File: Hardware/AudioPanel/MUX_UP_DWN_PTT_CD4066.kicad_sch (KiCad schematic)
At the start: 26 parts, among them SW8 ~{RESET}, U30 MCP23017_ML, U40 4066, U41 4066, U42 4066, U43 4066, U44 4066, U45 4066, U59 4066, U60 MCP23017_ML

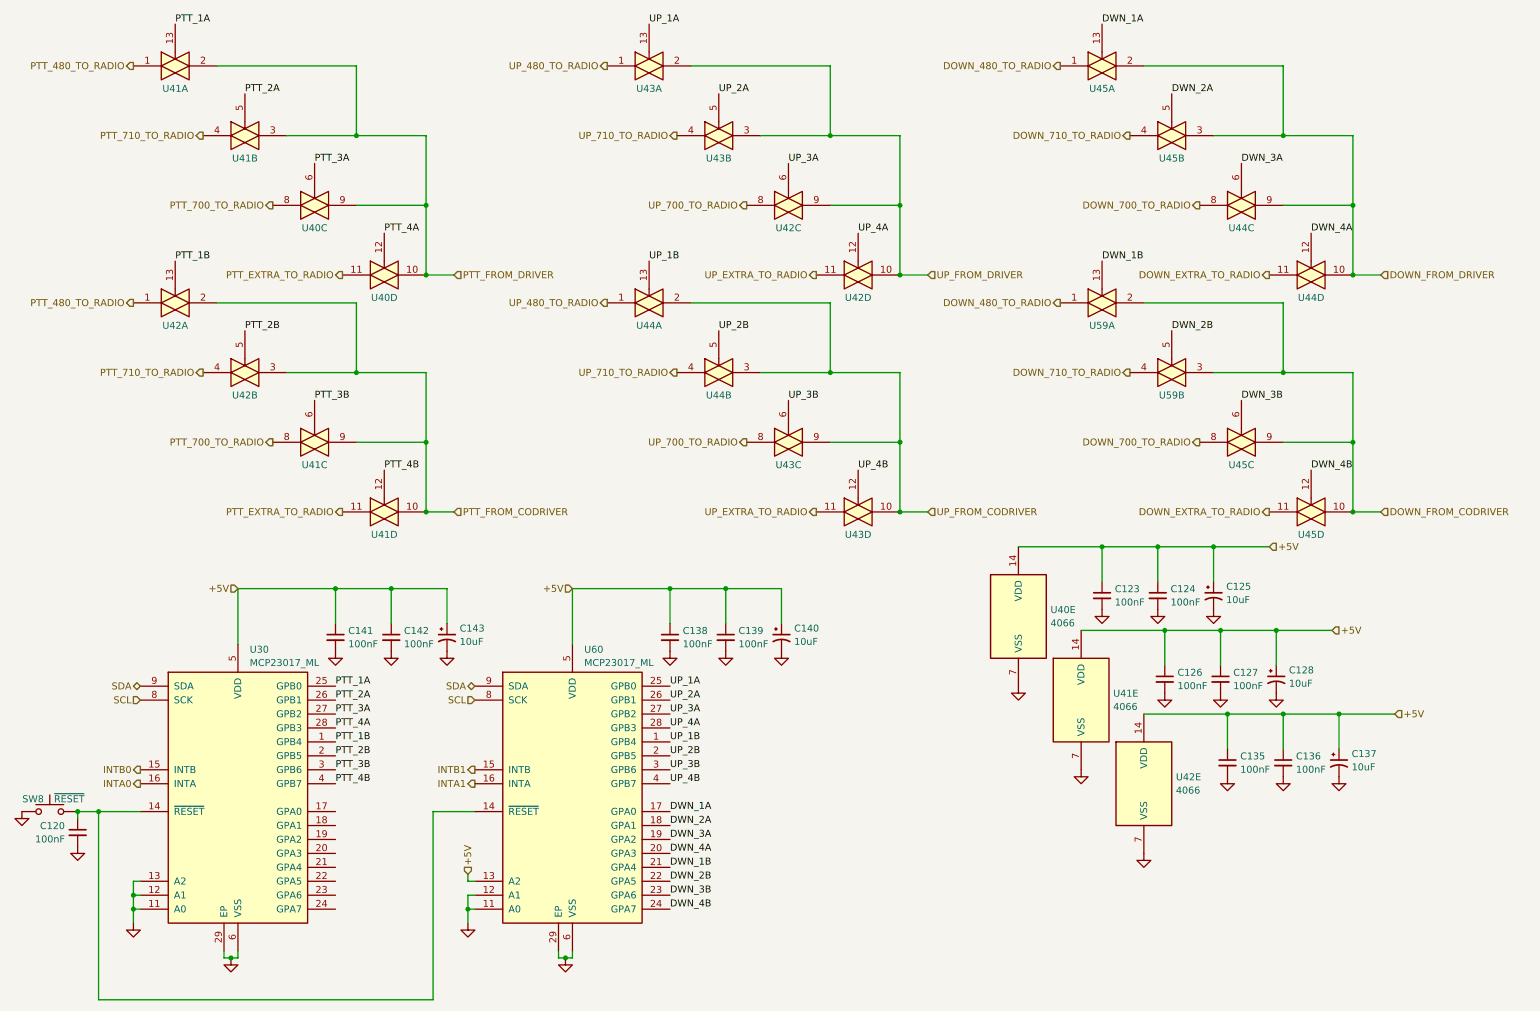
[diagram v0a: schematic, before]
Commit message: Added MIC port protection
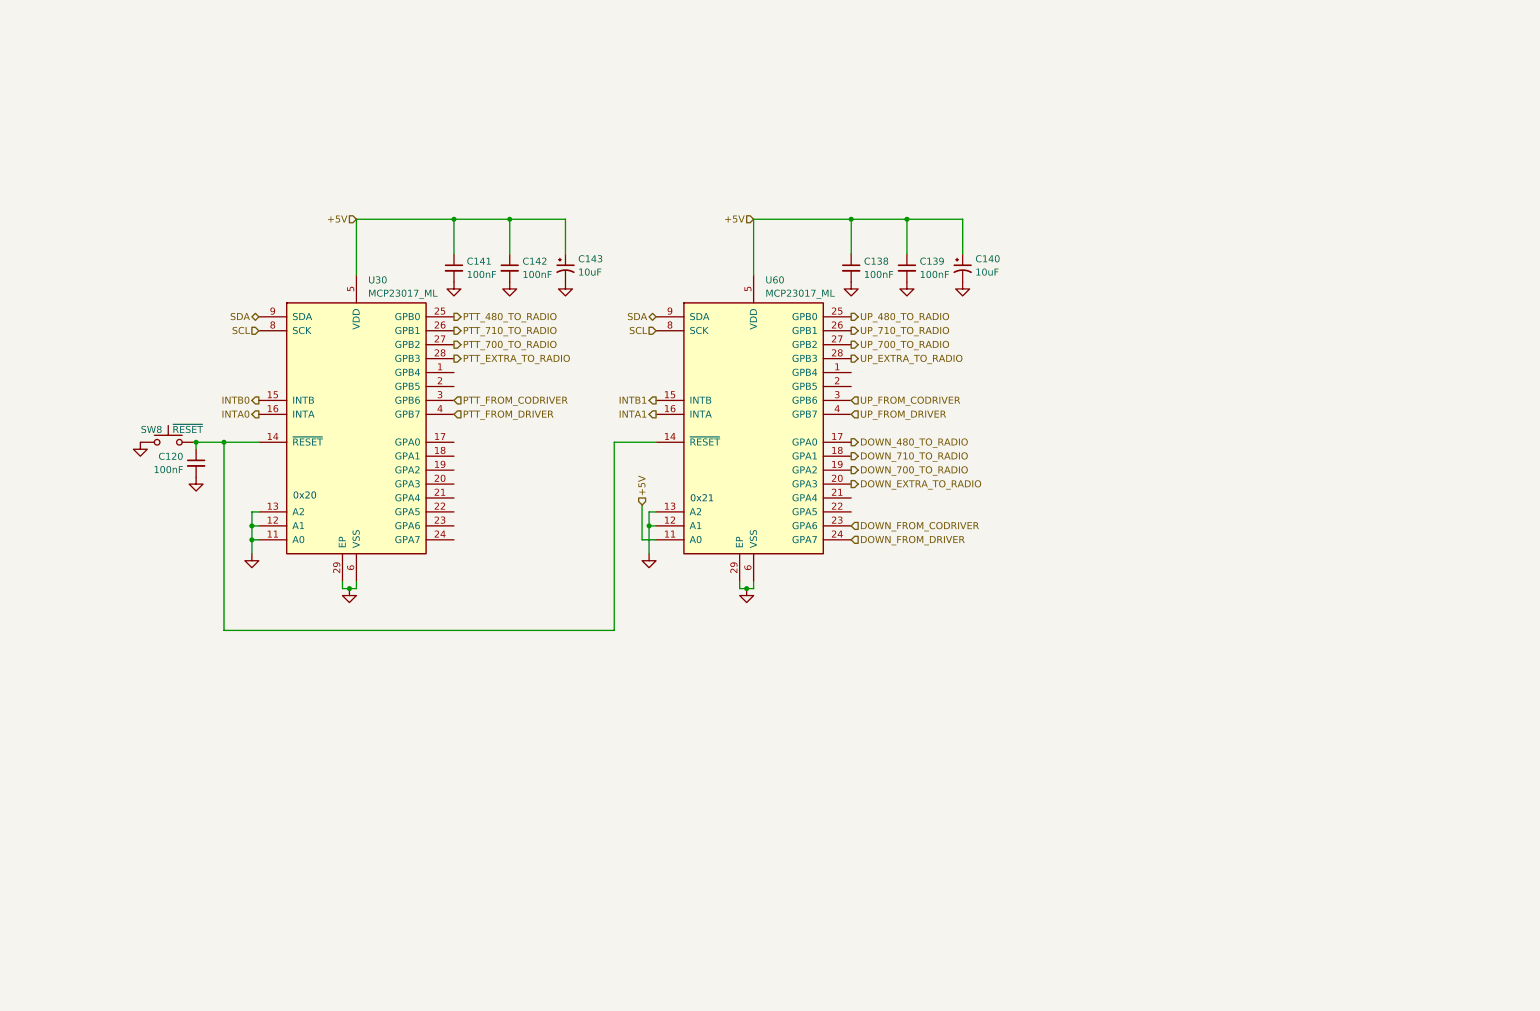
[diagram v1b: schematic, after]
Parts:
- removed C123, C124, C126, C127, C135, C136: 100nF, symbol Device:C_Small
- removed C125, C128, C137: 10uF, symbol Device:C_Polarized_Small_US
- removed U40, U41, U42, U43, U44, U45, U59: 4066, symbol 4xxx:4066
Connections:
- net DWN_1A is gone; now on net DOWN_480_TO_RADIO: U60.17 (GPA0)
- net DWN_2A is gone; now on net DOWN_710_TO_RADIO: U60.18 (GPA1)
- net DWN_3A is gone; now on net DOWN_700_TO_RADIO: U60.19 (GPA2)
- net DWN_3B is gone; now on net DOWN_FROM_CODRIVER: U60.23 (GPA6)
- net DWN_4A is gone; now on net DOWN_EXTRA_TO_RADIO: U60.20 (GPA3)
- net DWN_4B is gone; now on net DOWN_FROM_DRIVER: U60.24 (GPA7)
- net PTT_1A is gone; now on net PTT_480_TO_RADIO: U30.25 (GPB0)
- net PTT_2A is gone; now on net PTT_710_TO_RADIO: U30.26 (GPB1)
- net PTT_3A is gone; now on net PTT_700_TO_RADIO: U30.27 (GPB2)
- net PTT_3B is gone; now on net PTT_FROM_CODRIVER: U30.3 (GPB6)
- net PTT_4A is gone; now on net PTT_EXTRA_TO_RADIO: U30.28 (GPB3)
- net PTT_4B is gone; now on net PTT_FROM_DRIVER: U30.4 (GPB7)
- net UP_1A is gone; now on net UP_480_TO_RADIO: U60.25 (GPB0)
- net UP_2A is gone; now on net UP_710_TO_RADIO: U60.26 (GPB1)
- net UP_3A is gone; now on net UP_700_TO_RADIO: U60.27 (GPB2)
- net UP_3B is gone; now on net UP_FROM_CODRIVER: U60.3 (GPB6)
- net UP_4A is gone; now on net UP_EXTRA_TO_RADIO: U60.28 (GPB3)
- net UP_4B is gone; now on net UP_FROM_DRIVER: U60.4 (GPB7)
- net +5V: now also U60.11 (A0); no longer U60.13 (A2)
- net GND: now also U60.13 (A2); no longer U60.11 (A0)
- net DWN_1B: no longer names the net of U60.21 (GPA4)
- net DWN_2B: no longer names the net of U60.22 (GPA5)
- net PTT_1B: no longer names the net of U30.1 (GPB4)
- net PTT_2B: no longer names the net of U30.2 (GPB5)
- net UP_1B: no longer names the net of U60.1 (GPB4)
- net UP_2B: no longer names the net of U60.2 (GPB5)
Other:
- note added: "0x20"
- note added: "0x21"
- moved on the sheet: C120, C138, C139, C140, C141, C142, C143, SW8, U30, U60

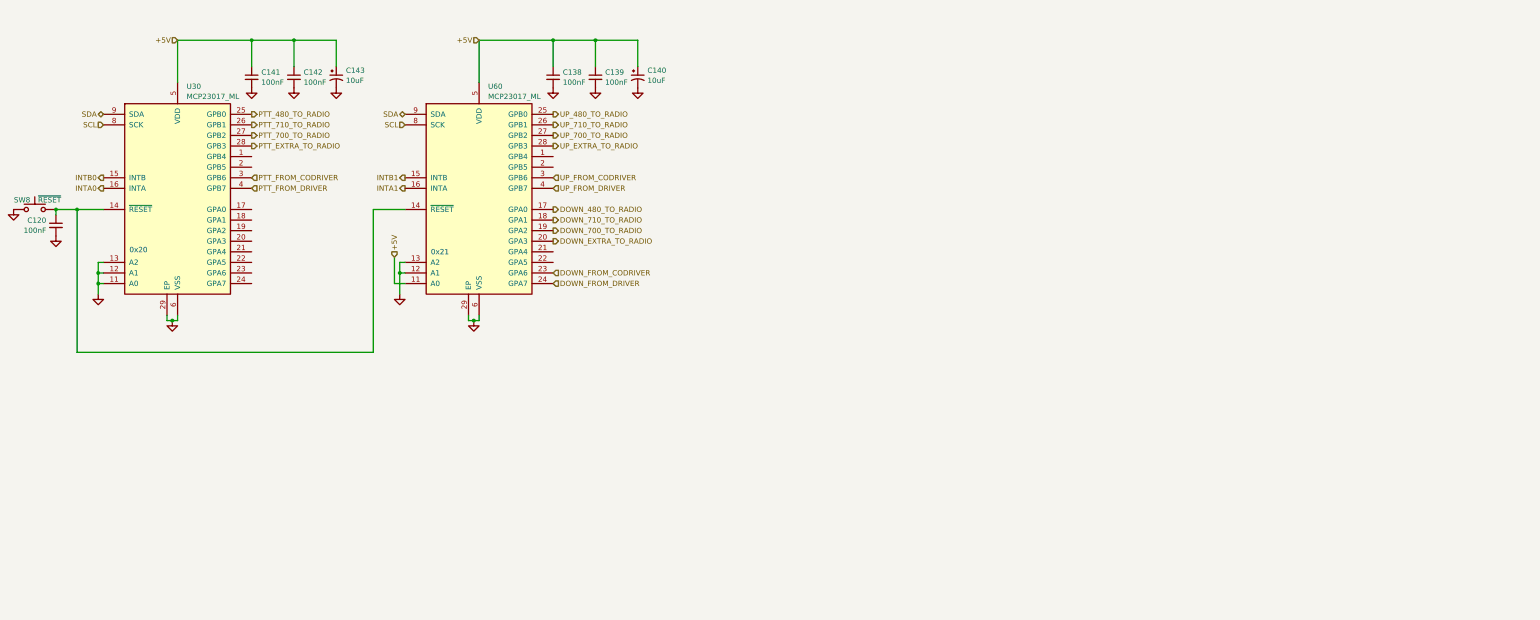
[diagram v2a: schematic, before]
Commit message: Added group labels
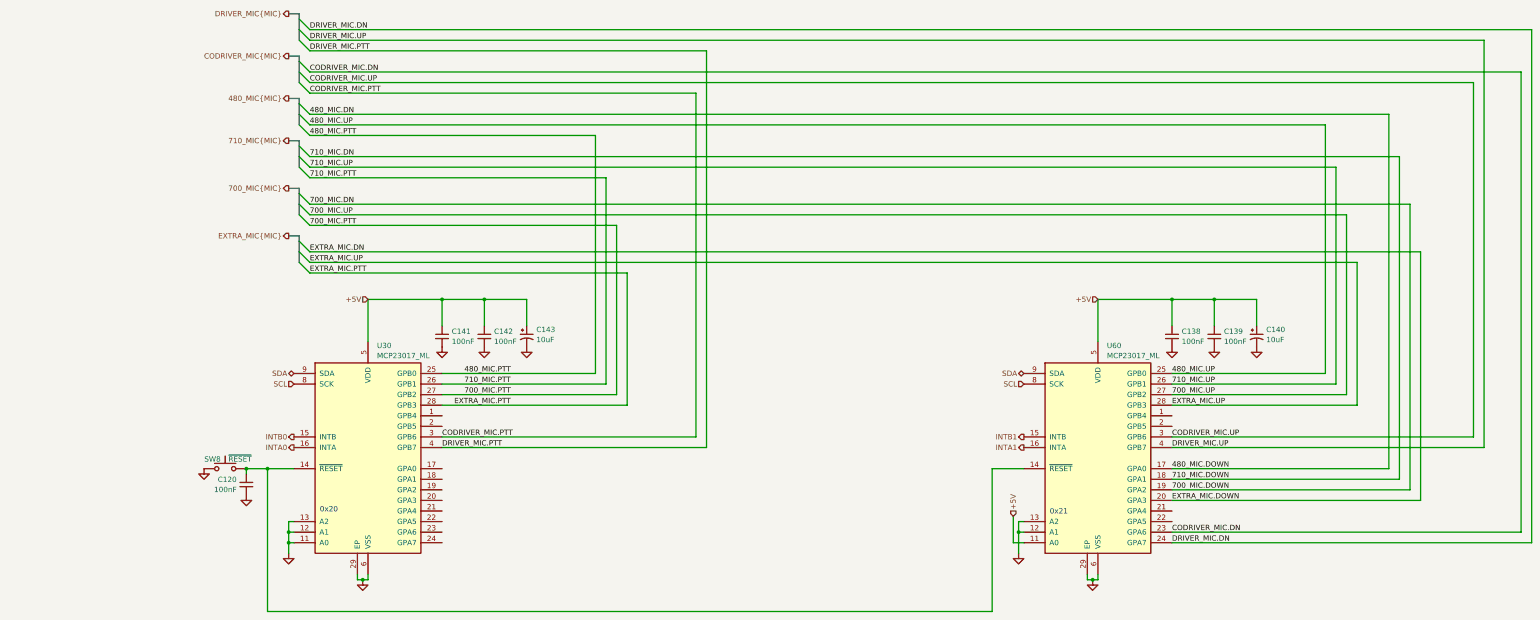
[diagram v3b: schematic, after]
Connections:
- net DOWN_480_TO_RADIO renamed 480_MIC.DN
- net DOWN_700_TO_RADIO renamed 700_MIC.DN
- net DOWN_710_TO_RADIO renamed 710_MIC.DN
- net DOWN_EXTRA_TO_RADIO renamed EXTRA_MIC.DN
- net DOWN_FROM_CODRIVER renamed CODRIVER_MIC.DN
- net DOWN_FROM_DRIVER renamed DRIVER_MIC.DN
- net PTT_480_TO_RADIO renamed 480_MIC.PTT
- net PTT_700_TO_RADIO renamed 700_MIC.PTT
- net PTT_710_TO_RADIO renamed 710_MIC.PTT
- net PTT_EXTRA_TO_RADIO renamed EXTRA_MIC.PTT
- net PTT_FROM_CODRIVER renamed CODRIVER_MIC.PTT
- net PTT_FROM_DRIVER renamed DRIVER_MIC.PTT
- net UP_480_TO_RADIO renamed 480_MIC.UP
- net UP_700_TO_RADIO renamed 700_MIC.UP
- net UP_710_TO_RADIO renamed 710_MIC.UP
- net UP_EXTRA_TO_RADIO renamed EXTRA_MIC.UP
- net UP_FROM_CODRIVER renamed CODRIVER_MIC.UP
- net UP_FROM_DRIVER renamed DRIVER_MIC.UP
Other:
- moved on the sheet: C120, C138, C139, C140, C141, C142, C143, SW8, U30, U60
